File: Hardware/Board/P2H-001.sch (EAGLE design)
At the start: 14 parts, among them IC1 74LS07N, IC2 LTC485N

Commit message: New board design.
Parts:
- added LED1: (no value), led:LED3MM
- added R5: 330, resistor:R-US_0204/5
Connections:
- new net N$20: R5.2, U$1.*5
- new net N$21: LED1.A, R5.1
- net GND: now also LED1.C
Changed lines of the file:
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@@
 <part name="SUPPLY10" library="supply2" deviceset="GND" device=""/>
 <part name="U$1" library="SparkFun-Boards" deviceset="ARDUINO_PRO_MINI" device=""/>
+<part name="R5" library="resistor" deviceset="R-US_" device="0204/5" value="330"/>
+<part name="LED1" library="led" deviceset="LED" device="3MM"/>
+<part name="SUPPLY11" library="supply2" deviceset="GND" device=""/>
 </parts>
 <sheets>
@@
 <instance part="SUPPLY10" gate="GND" x="223.52" y="-15.24"/>
 <instance part="U$1" gate="G$1" x="71.12" y="30.48"/>
+<instance part="R5" gate="G$1" x="40.64" y="27.94"/>
+<instance part="LED1" gate="G$1" x="33.02" y="22.86"/>
+<instance part="SUPPLY11" gate="GND" x="33.02" y="12.7"/>
 </instances>
 <busses>
@@
 <junction x="223.52" y="15.24"/>
 <junction x="223.52" y="27.94"/>
+</segment>
+<segment>
+<pinref part="LED1" gate="G$1" pin="C"/>
+<pinref part="SUPPLY11" gate="GND" pin="GND"/>
+<wire x1="33.02" y1="17.78" x2="33.02" y2="15.24" width="0.1524" layer="91"/>
 </segment>
 </net>
@@
 </segment>
 </net>
+<net name="N$20" class="0">
+<segment>
+<pinref part="U$1" gate="G$1" pin="*5"/>
+<pinref part="R5" gate="G$1" pin="2"/>
+<wire x1="60.96" y1="27.94" x2="45.72" y2="27.94" width="0.1524" layer="91"/>
+</segment>
+</net>
+<net name="N$21" class="0">
+<segment>
+<pinref part="R5" gate="G$1" pin="1"/>
+<pinref part="LED1" gate="G$1" pin="A"/>
+<wire x1="35.56" y1="27.94" x2="33.02" y2="27.94" width="0.1524" layer="91"/>
+<wire x1="33.02" y1="27.94" x2="33.02" y2="25.4" width="0.1524" layer="91"/>
+</segment>
+</net>

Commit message: Added comments.
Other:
- note added: "1,3: Power; 2, 4: GND 5-6: Reset 7-8: LED"
- note added: "1: Sensor X; 2: Sensor Y 3: GPIO; 4: MISO 5: MOSI; 6: SCLCK"
- note added: "1: TX+; 2: TX- 3: NC; 4: NC"
- note added: "1: Vcc; 2: GND 3: Sensor A; 4: Cable Detector"
- note added: "1: Vcc; 2: GND; 3: Raw TX 4: MIDI OUT Send; 5: MIDI OUT Return"
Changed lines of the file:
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@@
 <text x="154.94" y="-17.78" size="1.778" layer="91">Pineapple II Hydrogen 0.0.0
 Copyright 2015 by Pineapple.cc</text>
+<text x="119.38" y="68.58" size="1.778" layer="91">1: TX+; 2: TX-
+3: NC; 4: NC</text>
+<text x="10.16" y="88.9" size="1.778" layer="91">1: Vcc; 2: GND; 3: Raw TX
+4: MIDI OUT Send; 5: MIDI OUT Return</text>
+<text x="149.86" y="22.86" size="1.778" layer="91">1,3: Power; 2, 4: GND
+5-6: Reset
+7-8: LED</text>
+<text x="149.86" y="12.7" size="1.778" layer="91">1: Vcc; 2: GND
+3: Sensor A; 4: Cable Detector</text>
+<text x="149.86" y="0" size="1.778" layer="91">1: Sensor X; 2: Sensor Y
+3: GPIO; 4: MISO
+5: MOSI; 6: SCLCK</text>
 </plain>
 <instances>

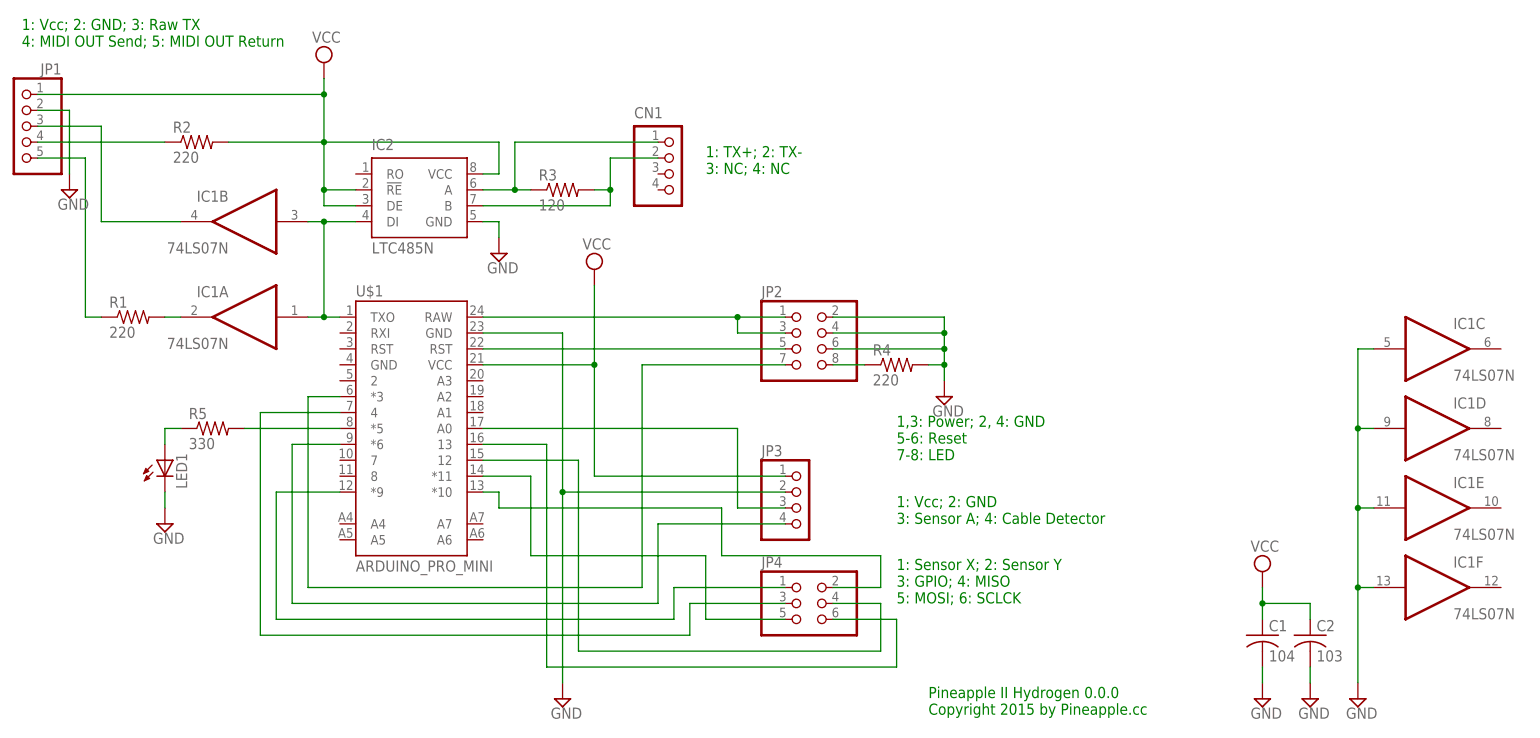
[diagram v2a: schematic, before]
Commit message: Changed board size to 45mm x 45mm.
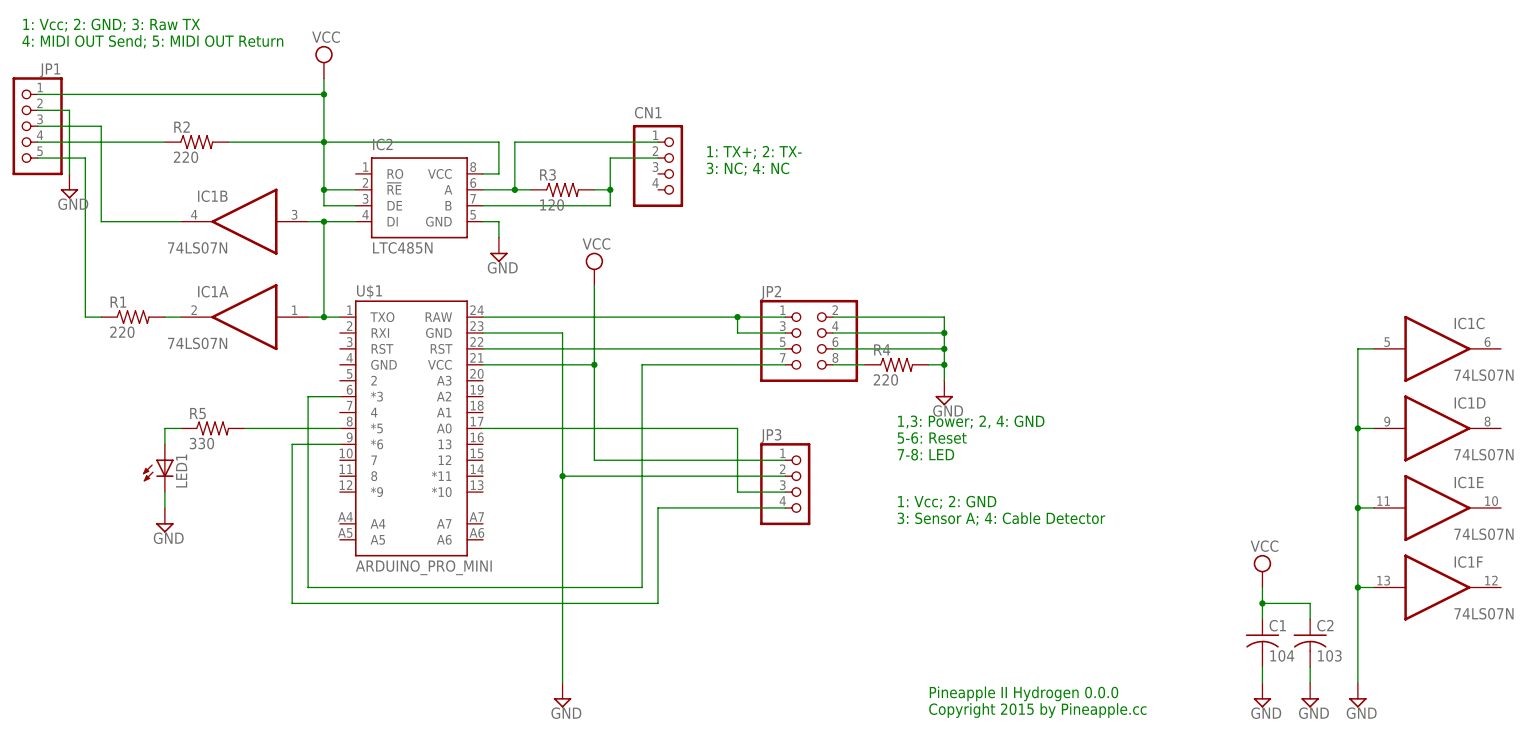
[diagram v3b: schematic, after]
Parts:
- removed JP4: (no value), pinhead:PINHD-2X3
- CN1: device jst-ph:S4B-PH-K-S -> jst-ph:B4B-PH-K-S
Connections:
- removed net N$12: JP4.1, U$1.*9
- removed net N$13: JP4.2, U$1.*10
- removed net N$14: JP4.3, U$1.4
- removed net N$15: JP4.4, U$1.12
- removed net N$16: JP4.5, U$1.*11
- removed net N$17: JP4.6, U$1.13
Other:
- note removed: "1: Sensor X; 2: Sensor Y 3: GPIO; 4: MISO 5: MOSI; 6: SCLCK"
- moved on the sheet: JP3
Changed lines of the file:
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@@
 <part name="R4" library="resistor" deviceset="R-US_" device="0204/5" value="220"/>
 <part name="JP3" library="pinhead" deviceset="PINHD-1X4" device=""/>
-<part name="JP4" library="pinhead" deviceset="PINHD-2X3" device=""/>
 <part name="IC2" library="linear-technology" deviceset="LTC485" device="N"/>
 <part name="R3" library="resistor" deviceset="R-US_" device="0204/5" value="120"/>
 <part name="SUPPLY3" library="supply2" deviceset="GND" device=""/>
-<part name="CN1" library="jst-ph" deviceset="S4B-PH-*" device="K-S"/>
+<part name="CN1" library="jst-ph" deviceset="B4B-PH-*" device="K-S"/>
 <part name="SUPPLY10" library="supply2" deviceset="GND" device=""/>
 <part name="U$1" library="SparkFun-Boards" deviceset="ARDUINO_PRO_MINI" device=""/>
@@
 <text x="149.86" y="12.7" size="1.778" layer="91">1: Vcc; 2: GND
 3: Sensor A; 4: Cable Detector</text>
-<text x="149.86" y="0" size="1.778" layer="91">1: Sensor X; 2: Sensor Y
-3: GPIO; 4: MISO
-5: MOSI; 6: SCLCK</text>
 </plain>
 <instances>
@@
 <instance part="SUPPLY6" gate="GND" x="157.48" y="33.02"/>
 <instance part="R4" gate="G$1" x="149.86" y="38.1"/>
-<instance part="JP3" gate="A" x="134.62" y="15.24"/>
-<instance part="JP4" gate="A" x="134.62" y="0"/>
+<instance part="JP3" gate="A" x="134.62" y="17.78"/>
 <instance part="IC2" gate="G$1" x="73.66" y="66.04"/>
 <instance part="R3" gate="G$1" x="96.52" y="66.04"/>
@@
 <segment>
 <wire x1="83.82" y1="43.18" x2="96.52" y2="43.18" width="0.1524" layer="91"/>
-<wire x1="96.52" y1="43.18" x2="96.52" y2="17.78" width="0.1524" layer="91"/>
+<wire x1="96.52" y1="43.18" x2="96.52" y2="20.32" width="0.1524" layer="91"/>
 <pinref part="SUPPLY4" gate="GND" pin="GND"/>
 <pinref part="JP3" gate="A" pin="2"/>
-<wire x1="96.52" y1="17.78" x2="96.52" y2="-12.7" width="0.1524" layer="91"/>
-<wire x1="132.08" y1="17.78" x2="96.52" y2="17.78" width="0.1524" layer="91"/>
-<junction x="96.52" y="17.78"/>
+<wire x1="96.52" y1="20.32" x2="96.52" y2="-12.7" width="0.1524" layer="91"/>
+<wire x1="132.08" y1="20.32" x2="96.52" y2="20.32" width="0.1524" layer="91"/>
+<junction x="96.52" y="20.32"/>
 <pinref part="U$1" gate="G$1" pin="GND@2"/>
 </segment>
@@
 <wire x1="83.82" y1="38.1" x2="101.6" y2="38.1" width="0.1524" layer="91"/>
 <wire x1="101.6" y1="38.1" x2="101.6" y2="50.8" width="0.1524" layer="91"/>
-<wire x1="101.6" y1="38.1" x2="101.6" y2="20.32" width="0.1524" layer="91"/>
+<wire x1="101.6" y1="38.1" x2="101.6" y2="22.86" width="0.1524" layer="91"/>
 <pinref part="JP3" gate="A" pin="1"/>
-<wire x1="101.6" y1="20.32" x2="132.08" y2="20.32" width="0.1524" layer="91"/>
+<wire x1="101.6" y1="22.86" x2="132.08" y2="22.86" width="0.1524" layer="91"/>
 <junction x="101.6" y="38.1"/>
 <pinref part="U$1" gate="G$1" pin="VCC"/>
@@
 <segment>
 <wire x1="83.82" y1="27.94" x2="124.46" y2="27.94" width="0.1524" layer="91"/>
-<wire x1="124.46" y1="27.94" x2="124.46" y2="15.24" width="0.1524" layer="91"/>
+<wire x1="124.46" y1="27.94" x2="124.46" y2="17.78" width="0.1524" layer="91"/>
 <pinref part="JP3" gate="A" pin="3"/>
-<wire x1="124.46" y1="15.24" x2="132.08" y2="15.24" width="0.1524" layer="91"/>
+<wire x1="124.46" y1="17.78" x2="132.08" y2="17.78" width="0.1524" layer="91"/>
 <pinref part="U$1" gate="G$1" pin="A0"/>
 </segment>
@@
 <wire x1="53.34" y1="25.4" x2="53.34" y2="0" width="0.1524" layer="91"/>
 <wire x1="53.34" y1="0" x2="111.76" y2="0" width="0.1524" layer="91"/>
-<wire x1="111.76" y1="0" x2="111.76" y2="12.7" width="0.1524" layer="91"/>
+<wire x1="111.76" y1="0" x2="111.76" y2="15.24" width="0.1524" layer="91"/>
 <pinref part="JP3" gate="A" pin="4"/>
-<wire x1="111.76" y1="12.7" x2="132.08" y2="12.7" width="0.1524" layer="91"/>
+<wire x1="111.76" y1="15.24" x2="132.08" y2="15.24" width="0.1524" layer="91"/>
 <pinref part="U$1" gate="G$1" pin="*6"/>
 </segment>
 </net>
-<net name="N$12" class="0">
-<segment>
-<wire x1="60.96" y1="17.78" x2="50.8" y2="17.78" width="0.1524" layer="91"/>
-<wire x1="50.8" y1="17.78" x2="50.8" y2="-2.54" width="0.1524" layer="91"/>
-<wire x1="50.8" y1="-2.54" x2="114.3" y2="-2.54" width="0.1524" layer="91"/>
-<wire x1="114.3" y1="-2.54" x2="114.3" y2="2.54" width="0.1524" layer="91"/>
-<pinref part="JP4" gate="A" pin="1"/>
-<wire x1="114.3" y1="2.54" x2="132.08" y2="2.54" width="0.1524" layer="91"/>
-<pinref part="U$1" gate="G$1" pin="*9"/>
-</segment>
-</net>
-<net name="N$13" class="0">
-<segment>
-<wire x1="83.82" y1="17.78" x2="86.36" y2="17.78" width="0.1524" layer="91"/>
-<wire x1="86.36" y1="17.78" x2="86.36" y2="15.24" width="0.1524" layer="91"/>
-<wire x1="86.36" y1="15.24" x2="121.92" y2="15.24" width="0.1524" layer="91"/>
-<wire x1="121.92" y1="15.24" x2="121.92" y2="7.62" width="0.1524" layer="91"/>
-<wire x1="121.92" y1="7.62" x2="147.32" y2="7.62" width="0.1524" layer="91"/>
-<wire x1="147.32" y1="7.62" x2="147.32" y2="2.54" width="0.1524" layer="91"/>
-<pinref part="JP4" gate="A" pin="2"/>
-<wire x1="147.32" y1="2.54" x2="139.7" y2="2.54" width="0.1524" layer="91"/>
-<pinref part="U$1" gate="G$1" pin="*10"/>
-</segment>
-</net>
-<net name="N$14" class="0">
-<segment>
-<wire x1="60.96" y1="30.48" x2="48.26" y2="30.48" width="0.1524" layer="91"/>
-<wire x1="48.26" y1="30.48" x2="48.26" y2="-5.08" width="0.1524" layer="91"/>
-<wire x1="48.26" y1="-5.08" x2="116.84" y2="-5.08" width="0.1524" layer="91"/>
-<wire x1="116.84" y1="-5.08" x2="116.84" y2="0" width="0.1524" layer="91"/>
-<pinref part="JP4" gate="A" pin="3"/>
-<wire x1="116.84" y1="0" x2="132.08" y2="0" width="0.1524" layer="91"/>
-<pinref part="U$1" gate="G$1" pin="4"/>
-</segment>
-</net>
-<net name="N$15" class="0">
-<segment>
-<wire x1="83.82" y1="22.86" x2="99.06" y2="22.86" width="0.1524" layer="91"/>
-<wire x1="99.06" y1="22.86" x2="99.06" y2="-7.62" width="0.1524" layer="91"/>
-<wire x1="99.06" y1="-7.62" x2="147.32" y2="-7.62" width="0.1524" layer="91"/>
-<wire x1="147.32" y1="-7.62" x2="147.32" y2="0" width="0.1524" layer="91"/>
-<pinref part="JP4" gate="A" pin="4"/>
-<wire x1="147.32" y1="0" x2="139.7" y2="0" width="0.1524" layer="91"/>
-<pinref part="U$1" gate="G$1" pin="12"/>
-</segment>
-</net>
-<net name="N$16" class="0">
-<segment>
-<wire x1="83.82" y1="20.32" x2="91.44" y2="20.32" width="0.1524" layer="91"/>
-<wire x1="91.44" y1="20.32" x2="91.44" y2="7.62" width="0.1524" layer="91"/>
-<wire x1="91.44" y1="7.62" x2="119.38" y2="7.62" width="0.1524" layer="91"/>
-<wire x1="119.38" y1="7.62" x2="119.38" y2="-2.54" width="0.1524" layer="91"/>
-<pinref part="JP4" gate="A" pin="5"/>
-<wire x1="119.38" y1="-2.54" x2="132.08" y2="-2.54" width="0.1524" layer="91"/>
-<pinref part="U$1" gate="G$1" pin="*11"/>
-</segment>
-</net>
-<net name="N$17" class="0">
-<segment>
-<wire x1="83.82" y1="25.4" x2="93.98" y2="25.4" width="0.1524" layer="91"/>
-<wire x1="93.98" y1="25.4" x2="93.98" y2="-10.16" width="0.1524" layer="91"/>
-<wire x1="93.98" y1="-10.16" x2="149.86" y2="-10.16" width="0.1524" layer="91"/>
-<wire x1="149.86" y1="-10.16" x2="149.86" y2="-2.54" width="0.1524" layer="91"/>
-<pinref part="JP4" gate="A" pin="6"/>
-<wire x1="149.86" y1="-2.54" x2="139.7" y2="-2.54" width="0.1524" layer="91"/>
-<pinref part="U$1" gate="G$1" pin="13"/>
-</segment>
-</net>

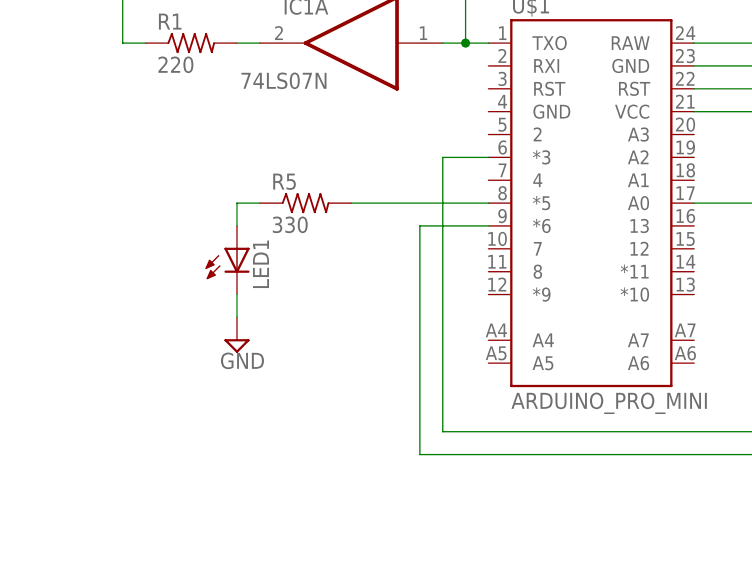
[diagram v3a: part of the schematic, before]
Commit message: Changed position of LED resistor.
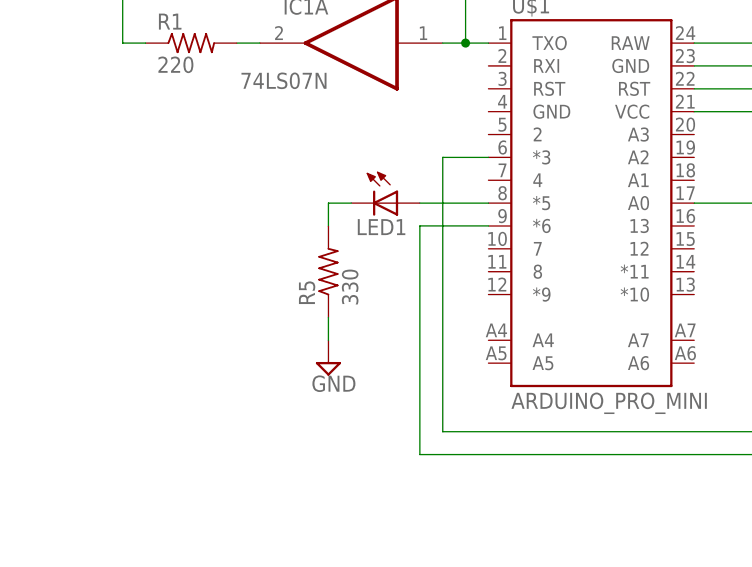
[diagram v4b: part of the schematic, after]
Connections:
- removed net N$20: R5.2, U$1.*5
- removed net N$21: LED1.A, R5.1
- new net N$12: LED1.A, U$1.*5
- new net N$13: LED1.C, R5.2
- net GND: now also R5.1; no longer LED1.C
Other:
- moved on the sheet: LED1, R5
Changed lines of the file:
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@@
 <instance part="SUPPLY10" gate="GND" x="223.52" y="-15.24"/>
 <instance part="U$1" gate="G$1" x="71.12" y="30.48"/>
-<instance part="R5" gate="G$1" x="40.64" y="27.94"/>
-<instance part="LED1" gate="G$1" x="33.02" y="22.86"/>
-<instance part="SUPPLY11" gate="GND" x="33.02" y="12.7"/>
+<instance part="R5" gate="G$1" x="43.18" y="20.32" rot="R90"/>
+<instance part="LED1" gate="G$1" x="50.8" y="27.94" rot="R270"/>
+<instance part="SUPPLY11" gate="GND" x="43.18" y="10.16"/>
 </instances>
 <busses>
@@
 </segment>
 <segment>
-<pinref part="LED1" gate="G$1" pin="C"/>
 <pinref part="SUPPLY11" gate="GND" pin="GND"/>
-<wire x1="33.02" y1="17.78" x2="33.02" y2="15.24" width="0.1524" layer="91"/>
+<pinref part="R5" gate="G$1" pin="1"/>
+<wire x1="43.18" y1="15.24" x2="43.18" y2="12.7" width="0.1524" layer="91"/>
 </segment>
 </net>
@@
 </segment>
 </net>
-<net name="N$20" class="0">
+<net name="N$12" class="0">
 <segment>
 <pinref part="U$1" gate="G$1" pin="*5"/>
+<pinref part="LED1" gate="G$1" pin="A"/>
+<wire x1="60.96" y1="27.94" x2="53.34" y2="27.94" width="0.1524" layer="91"/>
+</segment>
+</net>
+<net name="N$13" class="0">
+<segment>
+<pinref part="LED1" gate="G$1" pin="C"/>
 <pinref part="R5" gate="G$1" pin="2"/>
-<wire x1="60.96" y1="27.94" x2="45.72" y2="27.94" width="0.1524" layer="91"/>
-</segment>
-</net>
-<net name="N$21" class="0">
-<segment>
-<pinref part="R5" gate="G$1" pin="1"/>
-<pinref part="LED1" gate="G$1" pin="A"/>
-<wire x1="35.56" y1="27.94" x2="33.02" y2="27.94" width="0.1524" layer="91"/>
-<wire x1="33.02" y1="27.94" x2="33.02" y2="25.4" width="0.1524" layer="91"/>
-</segment>
-</net>
+<wire x1="45.72" y1="27.94" x2="43.18" y2="27.94" width="0.1524" layer="91"/>
+<wire x1="43.18" y1="27.94" x2="43.18" y2="25.4" width="0.1524" layer="91"/>
+</segment>
+</net>
